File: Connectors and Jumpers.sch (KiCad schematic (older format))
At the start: 11 parts, among them J11 USB_A, J3 Conn_02x03_Odd_Even, J4 Conn_02x09_Odd_Even, J5 Conn_01x02, J6 Conn_01x02, J7 Screw_Terminal_01x02, J8 Micro_SD_Card, J9 Conn_01x02

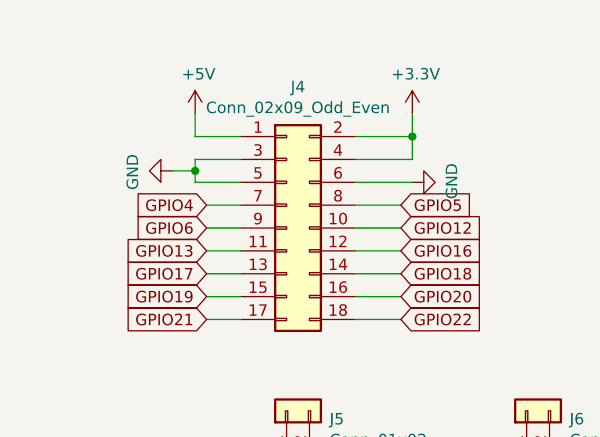
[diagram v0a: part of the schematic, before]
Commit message: 5V connection point increased
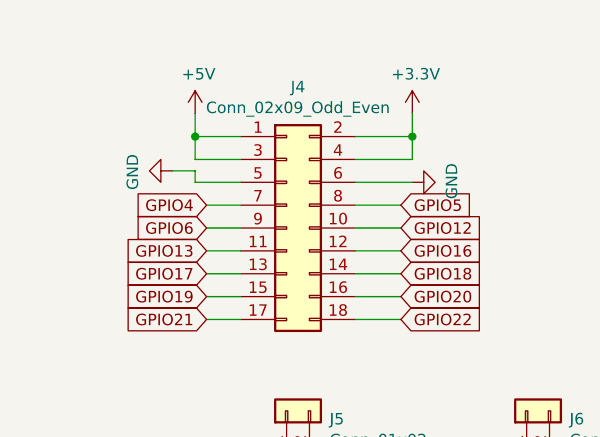
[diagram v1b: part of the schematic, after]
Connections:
- net +5V: now also J4.3 (Pin_3)
- net GND: no longer J4.3 (Pin_3)
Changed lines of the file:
@@
 	1250 2100 1450 2100
 Wire Wire Line
-	1250 2200 1250 2250
-Wire Wire Line
 	1250 2300 1450 2300
-Wire Wire Line
-	1250 2200 1450 2200
 $Comp
 L power:GND #PWR0155
@@
 Wire Wire Line
 	1150 2250 1250 2250
-Connection ~ 1250 2250
 Wire Wire Line
 	1250 2250 1250 2300
@@
 Text GLabel 3950 3550 3    50   Input ~ 0
 RXD1
+Wire Wire Line
+	1250 2100 1250 2200
+Wire Wire Line
+	1250 2200 1450 2200
+Connection ~ 1250 2100
 $EndSCHEMATC

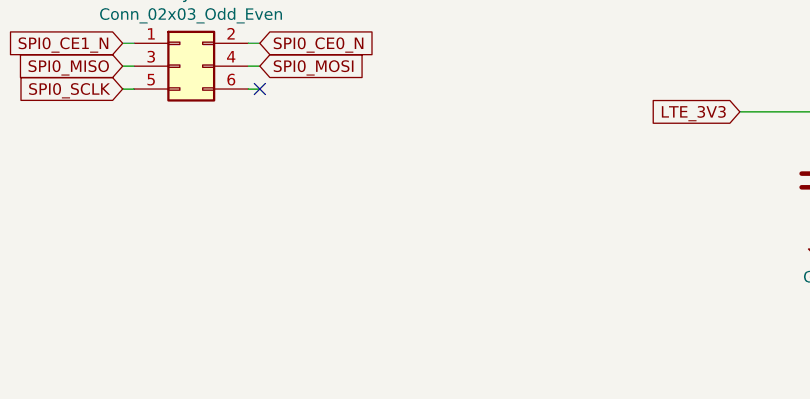
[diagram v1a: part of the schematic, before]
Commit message: USB pinHeader added
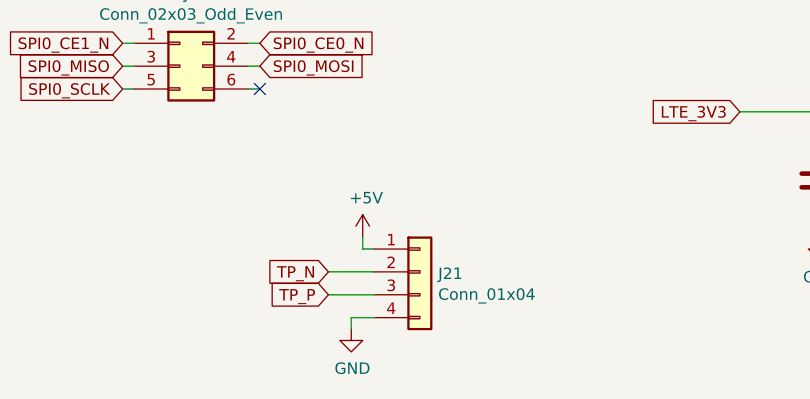
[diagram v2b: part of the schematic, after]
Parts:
- added J21: Conn_01x04, Connector_PinSocket_2.54mm:PinSocket_1x04_P2.54mm_Vertical, symbol Connector_Generic:Conn_01x04
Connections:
- net +5V: now also J21.1 (Pin_1)
- net GND: now also J21.4 (Pin_4)
- new net TP_N: J21.2 (Pin_2)
- new net TP_P: J21.3 (Pin_3)
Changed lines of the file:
@@
 	1250 2200 1450 2200
 Connection ~ 1250 2100
+$Comp
+L Connector_Generic:Conn_01x04 J21
+U 1 1 62C7FE11
+P 2400 5300
+F 0 "J21" H 2480 5292 50  0000 L CNN
+F 1 "Conn_01x04" H 2480 5201 50  0000 L CNN
+F 2 "Connector_PinSocket_2.54mm:PinSocket_1x04_P2.54mm_Vertical" H 2400 5300 50  0001 C CNN
+F 3 "~" H 2400 5300 50  0001 C CNN
+	1    2400 5300
+	1    0    0    -1
+$EndComp
+Wire Wire Line
+	2200 5300 2000 5300
+Text GLabel 2000 5300 0    50   Input ~ 0
+TP_N
+Wire Wire Line
+	2200 5400 2000 5400
+Text GLabel 2000 5400 0    50   Input ~ 0
+TP_P
+$Comp
+L power:GND #PWR0147
+U 1 1 62C8C13E
+P 2100 5550
+F 0 "#PWR0147" H 2100 5300 50  0001 C CNN
+F 1 "GND" H 2105 5377 50  0000 C CNN
+F 2 "" H 2100 5550 50  0001 C CNN
+F 3 "" H 2100 5550 50  0001 C CNN
+	1    2100 5550
+	1    0    0    -1
+$EndComp
+Wire Wire Line
+	2100 5550 2100 5500
+Wire Wire Line
+	2100 5500 2200 5500
+$Comp
+L power:+5V #PWR0156
+U 1 1 62C8EF7E
+P 2150 5150
+F 0 "#PWR0156" H 2150 5000 50  0001 C CNN
+F 1 "+5V" H 2165 5323 50  0000 C CNN
+F 2 "" H 2150 5150 50  0001 C CNN
+F 3 "" H 2150 5150 50  0001 C CNN
+	1    2150 5150
+	1    0    0    -1
+$EndComp
+Wire Wire Line
+	2150 5150 2150 5200
+Wire Wire Line
+	2150 5200 2200 5200
 $EndSCHEMATC
